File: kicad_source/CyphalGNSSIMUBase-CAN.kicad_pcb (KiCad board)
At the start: 2 copper layers, 52 x 36 mm, 39 parts, among them CN1 RASPBERRYPI_PICO, CN2 SM04B-SRSS-TB, CN3 SM04B-SRSS-TB, CN4 SM04B-GHS-TB, CN5 SM04B-GHS-TB, SW1 PTS636 SM43 SMTR LFS, U3 M24C64-RMN6TP, U8 MCP2515T-I/SO, U9 SN65HVD230, Y1 X322516MLB4SI

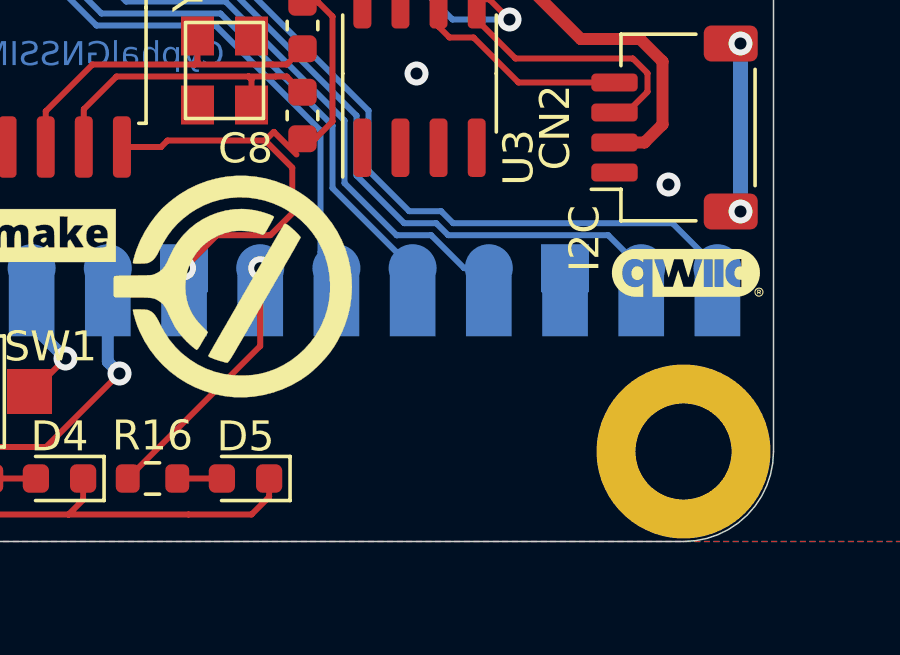
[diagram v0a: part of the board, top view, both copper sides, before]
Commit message: added BNO085
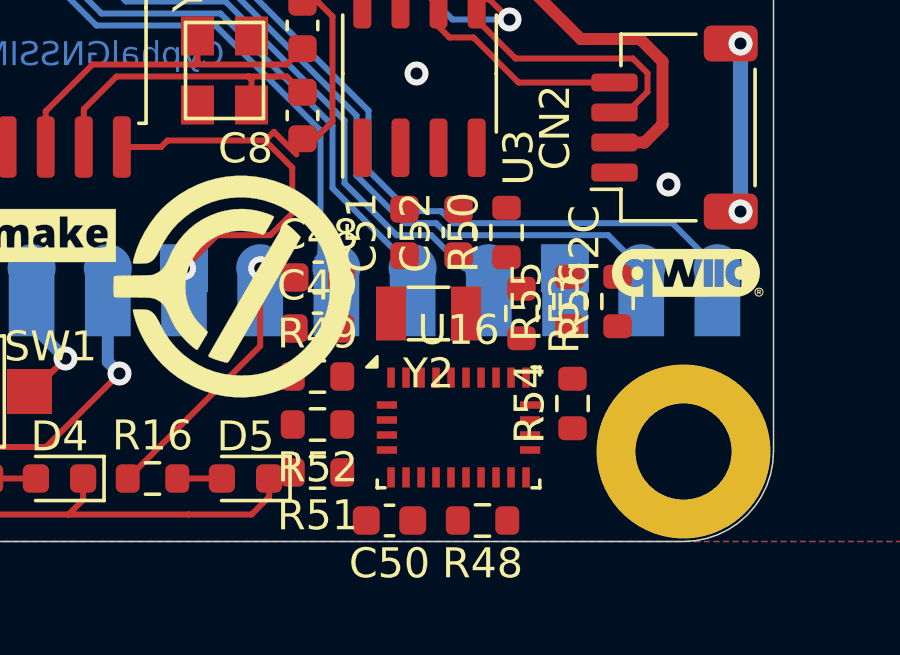
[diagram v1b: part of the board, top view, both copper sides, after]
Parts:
- added C48: 100nF, Capacitor_SMD:C_0603_1608Metric, F.Cu at (100.8, 101.2)
- added C49: 100nF, Capacitor_SMD:C_0603_1608Metric, F.Cu at (100.8, 102.9)
- added C50: 100nF, Capacitor_SMD:C_0603_1608Metric, F.Cu at (103.2, 109.3)
- added C51: 22pF, Capacitor_SMD:C_0603_1608Metric, F.Cu at (103.7, 99.7)
- added C52: 22pF, Capacitor_SMD:C_0603_1608Metric, F.Cu at (105.5, 99.7)
- added R48: 0R, Resistor_SMD:R_0603_1608Metric, F.Cu at (106.3, 109.3)
- added R49: 10k, Resistor_SMD:R_0603_1608Metric, F.Cu at (100.8, 104.5)
- added R50: 0R, Resistor_SMD:R_0603_1608Metric, F.Cu at (107.1, 99.7)
- added R51: 0R, Resistor_SMD:R_0603_1608Metric, F.Cu at (100.8, 107.7)
- added R52: 0R, Resistor_SMD:R_0603_1608Metric, F.Cu at (100.8, 106.1)
- added R53: DNI, Resistor_SMD:R_0603_1608Metric, F.Cu at (107.6, 102.4)
- added R54: 0R, Resistor_SMD:R_0603_1608Metric, F.Cu at (109.3, 105.4)
- added R55: DNI, Resistor_SMD:R_0603_1608Metric, F.Cu at (109.2, 102.0)
- added R56: DNI, Resistor_SMD:R_0603_1608Metric, F.Cu at (110.8, 102.0)
- added U16: BNO085, Package_LGA:LGA-28_5.2x3.8mm_P0.5mm, F.Cu at (105.5, 106.2)
- added Y2: DNI, Crystal:Crystal_SMD_3215-2Pin_3.2x1.5mm, F.Cu at (104.5, 102.4)
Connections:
- net /I2C_SCL renamed I2C_SCL
- net /I2C_SDA renamed I2C_SDA
- D2 pad 1: Net-(D2-K) -> (no net)
- F1 pad 2: Net-(D2-K) -> (no net)
- U9 pad 5: unconnected-(U9-NC2-Pad5) -> (no net)
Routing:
- net Net-(D2-K): track 4.26 -> 0.00 mm
- net (no net): track 6.35 -> 10.6 mm

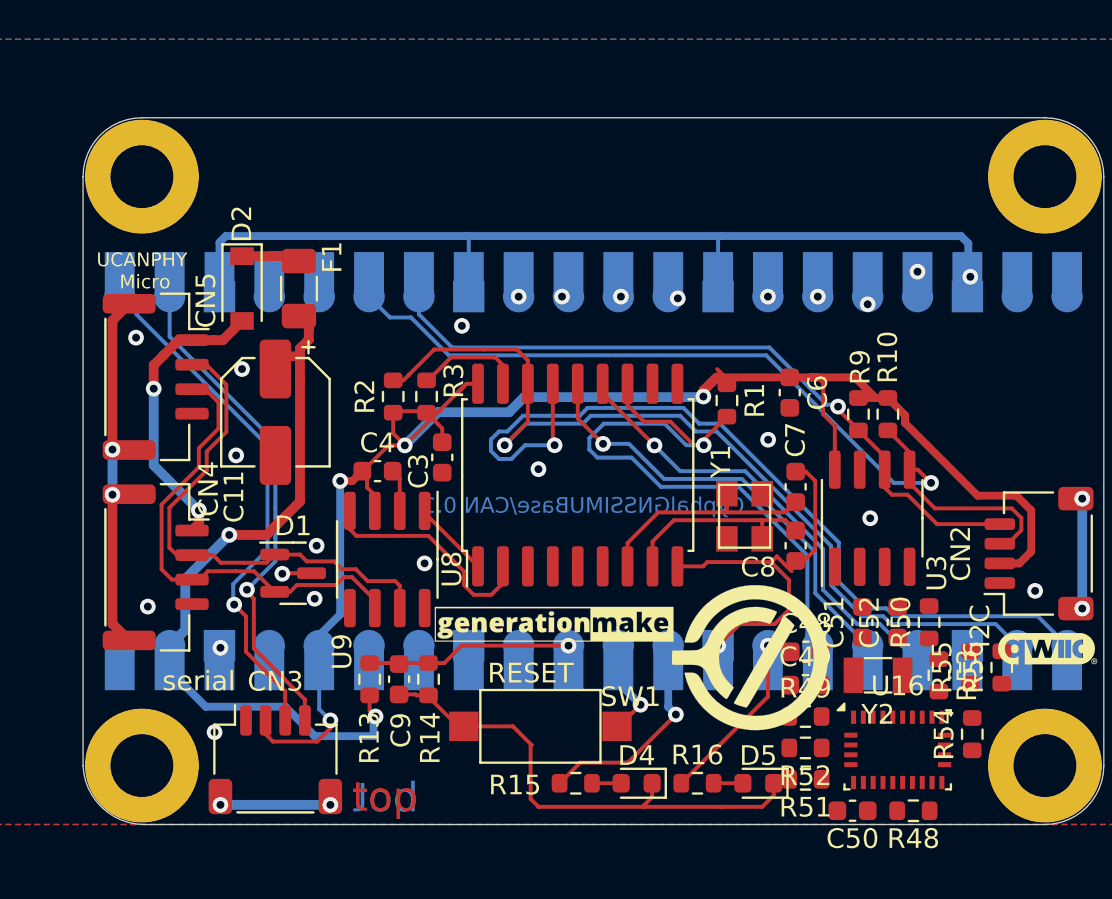
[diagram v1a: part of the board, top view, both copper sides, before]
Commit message: added GNSS u-blox max-m10
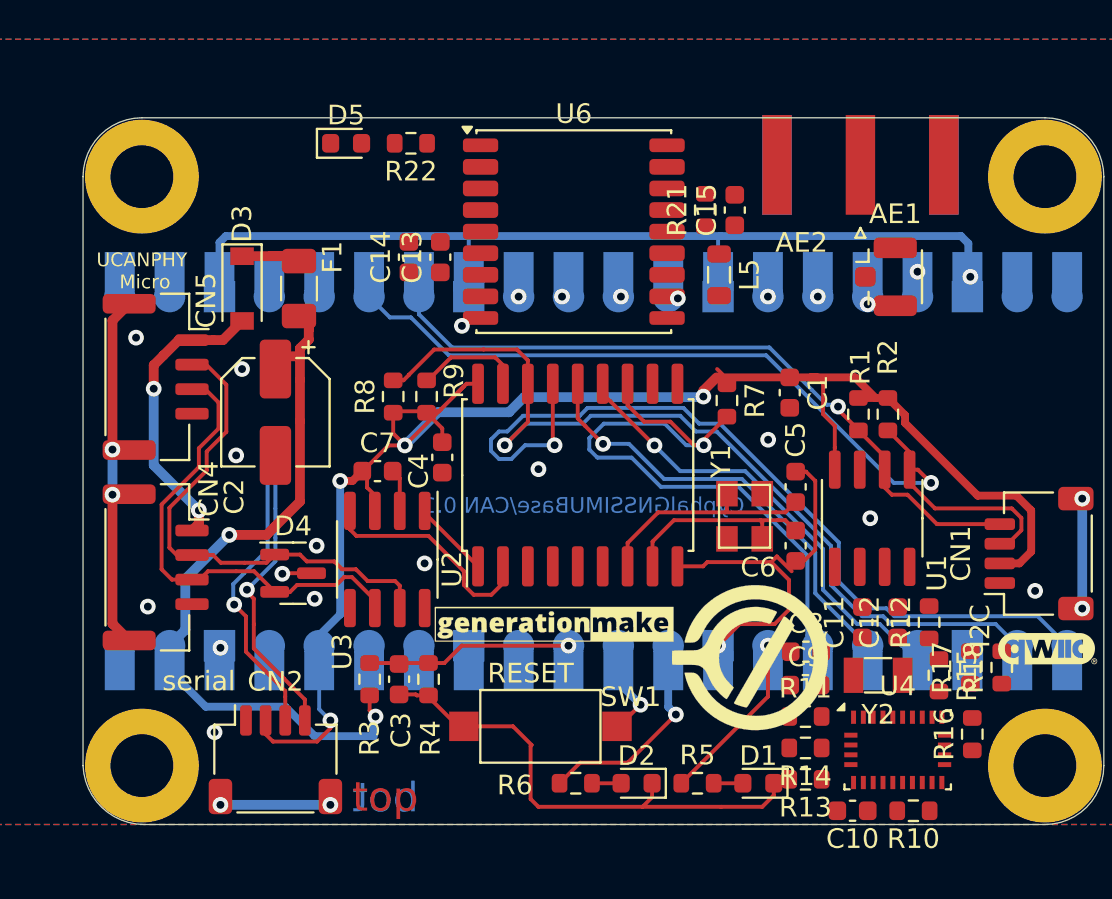
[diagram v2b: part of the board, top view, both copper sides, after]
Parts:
- added AE1: Antenna_Shield, Connector_Coaxial:U.FL_Hirose_U.FL-R-SMT-1_Vertical, F.Cu at (104.9, 82.1)
- added AE2: Antenna_Shield, Connector_Coaxial:SMA_Amphenol_132289_EdgeMount, F.Cu at (103.6, 76.4)
- added C13: 100 nF, Capacitor_SMD:C_0603_1608Metric, F.Cu at (82.2, 81.1)
- added C14: 100 nF, Capacitor_SMD:C_0603_1608Metric, F.Cu at (80.6, 81.1)
- added C15: 100 nF, Capacitor_SMD:C_0603_1608Metric, F.Cu at (97.2, 78.7)
- added D5: LED_Small, LED_SMD:LED_0603_1608Metric, F.Cu at (77.4, 75.3)
- added L5: L, Inductor_SMD:L_0805_2012Metric, F.Cu at (96.4, 82.0)
- added R21: 1k, Resistor_SMD:R_0603_1608Metric, F.Cu at (95.7, 78.7)
- added R22: 1k, Resistor_SMD:R_0603_1608Metric, F.Cu at (80.7, 75.3)
- added U6: MAX-M10S, RF_GPS:ublox_MAX, F.Cu at (89.0, 79.8)
- renumbered C6 to C1, C50 to C10, C51 to C11, C52 to C12, C11 to C2, C9 to C3, C3 to C4, C7 to C5, C8 to C6, C4 to C7, C48 to C8, C49 to C9, CN2 to CN1, CN3 to CN2, CN1 to CN3, D5 to D1, D4 to D2, D2 to D3, D1 to D4, R9 to R1, R48 to R10, R49 to R11, R50 to R12, R51 to R13, R52 to R14, R53 to R15, R54 to R16, R55 to R17, R56 to R18, R10 to R2, R13 to R3, R14 to R4, R16 to R5, R15 to R6, R1 to R7, R2 to R8, R3 to R9, U3 to U1, U8 to U2, U9 to U3, U16 to U4
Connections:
- CN2 pad 3: /SER_TX -> /SERIAL2_TX
- CN2 pad 4: /SER_RX -> /SERIAL2_RX
- CN3 pad 1: /SER_TX -> SERIAL1_TX
- CN3 pad 11: /INPUT2 -> /SERIAL2_TX
- CN3 pad 12: /INPUT3 -> /SERIAL2_RX
- CN3 pad 2: /SER_RX -> SERIAL1_RX
- D3 pad 1: (no net) -> Net-(D3-K)
- F1 pad 2: (no net) -> Net-(D3-K)
- U3 pad 5: (no net) -> unconnected-(U3-NC2-Pad5)
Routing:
- net /SER_TX: track 27.8 -> 0.00 mm, vias 1 -> 0
- net /SER_RX: track 27.0 -> 0.00 mm, vias 1 -> 0
- net /SERIAL2_TX: track 0.00 -> 17.1 mm, vias 0 -> 2
- net /SERIAL2_RX: track 0.00 -> 16.0 mm, vias 0 -> 1
- net Net-(D3-K): track 0.00 -> 4.26 mm
- net (no net): track 10.6 -> 6.35 mm
- net SERIAL1_TX: track 0.00 -> 1.27 mm
- net SERIAL1_RX: track 0.00 -> 1.27 mm
- net /INPUT3: track 1.27 -> 0.00 mm, vias 1 -> 0
- net /INPUT2: track 1.27 -> 0.00 mm, vias 1 -> 0
- net /GNSS/NEO_ANTENNA: track 0.00 -> 1.27 mm, vias 0 -> 1

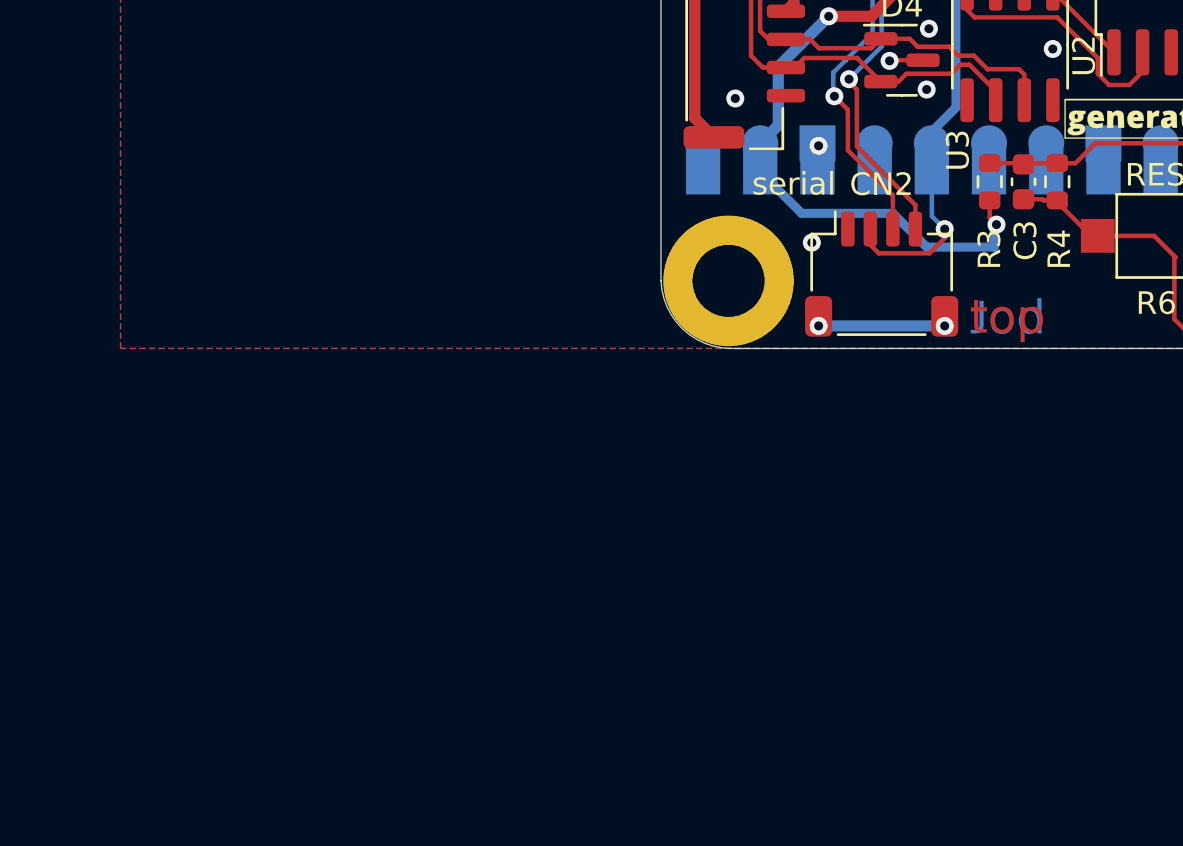
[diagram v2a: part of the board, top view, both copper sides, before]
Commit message: added RS232 level shifter
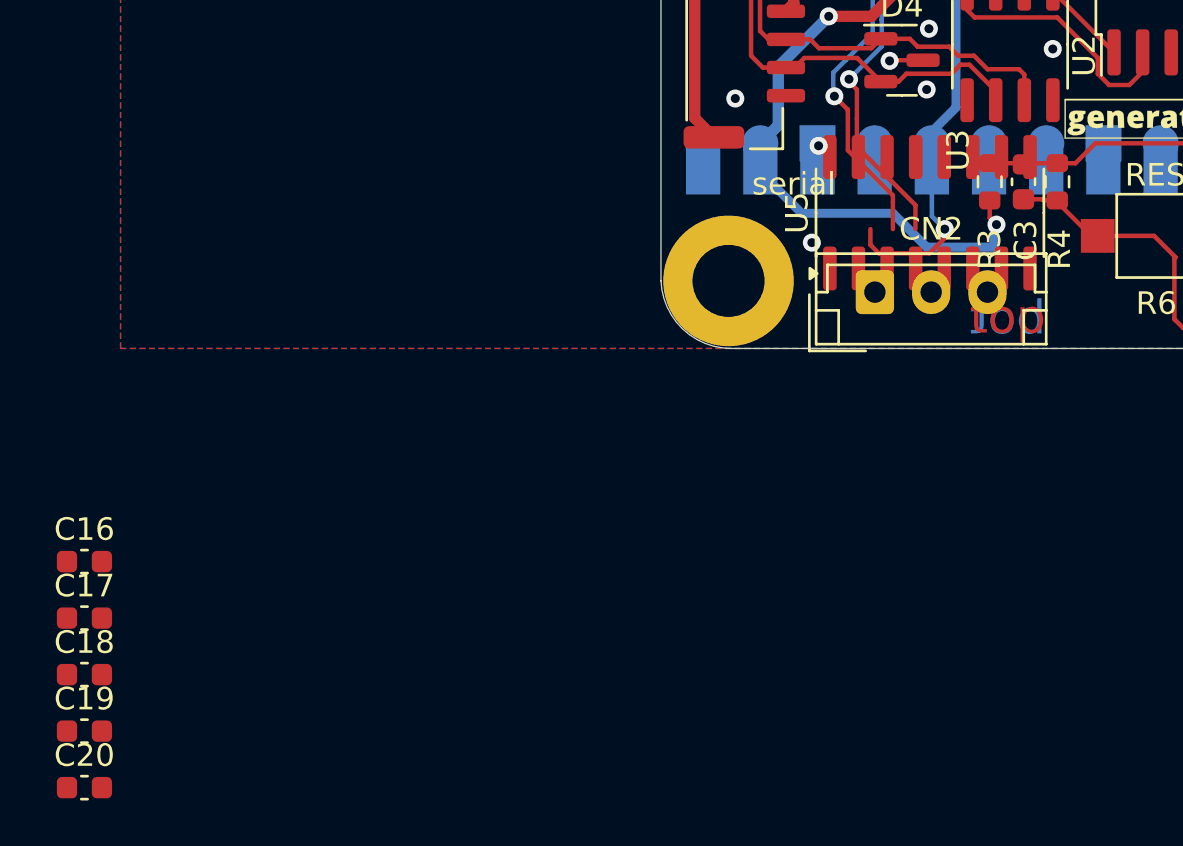
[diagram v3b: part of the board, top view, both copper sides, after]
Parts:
- added C16: 100nF, Capacitor_SMD:C_0603_1608Metric, F.Cu at (38.4, 119.5)
- added C17: 100nF, Capacitor_SMD:C_0603_1608Metric, F.Cu at (38.4, 122.0)
- added C18: 100nF, Capacitor_SMD:C_0603_1608Metric, F.Cu at (38.4, 124.5)
- added C19: 100nF, Capacitor_SMD:C_0603_1608Metric, F.Cu at (38.4, 127.0)
- added C20: 100nF, Capacitor_SMD:C_0603_1608Metric, F.Cu at (38.4, 129.5)
- added U5: MAX3232, Package_SO:SOIC-16_3.9x9.9mm_P1.27mm, F.Cu at (75.9, 104.0)
- CN2: value SM04B-SRSS-TB -> Conn_01x03; footprint generationmake:JST_SH_SM04B-SRSS-TB_1x04-1MP_P1.00mm_Horizontal -> Connector_JST:JST_EH_B3B-EH-A_1x03_P2.50mm_Vertical
- moved CN2 0.85 mm to (73.5, 107.5)
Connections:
- CN2 pad 1: GND -> /RS232_TX
- CN2 pad 2: +3V3 -> GND
- CN2 pad 3: /SERIAL2_TX -> /RS232_TX
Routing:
- net /MP3: track 5.60 -> 0.00 mm, vias 2 -> 0

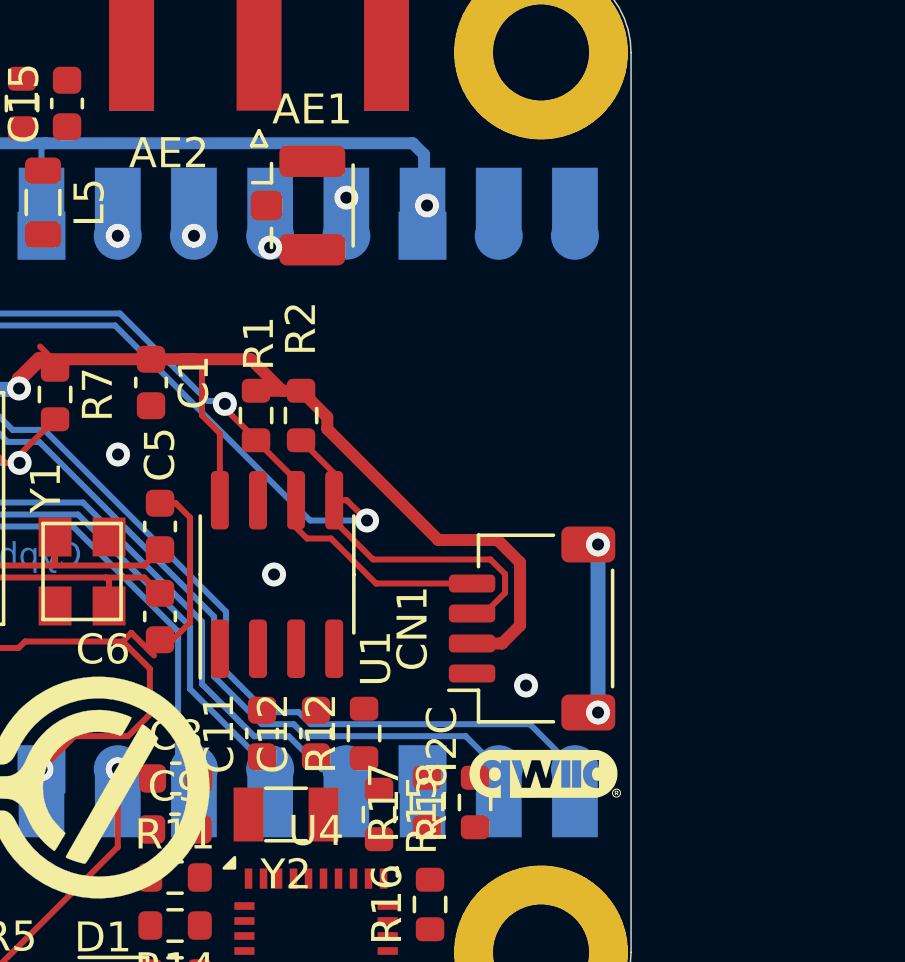
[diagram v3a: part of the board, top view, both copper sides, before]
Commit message: added battery holder for GNSS backup
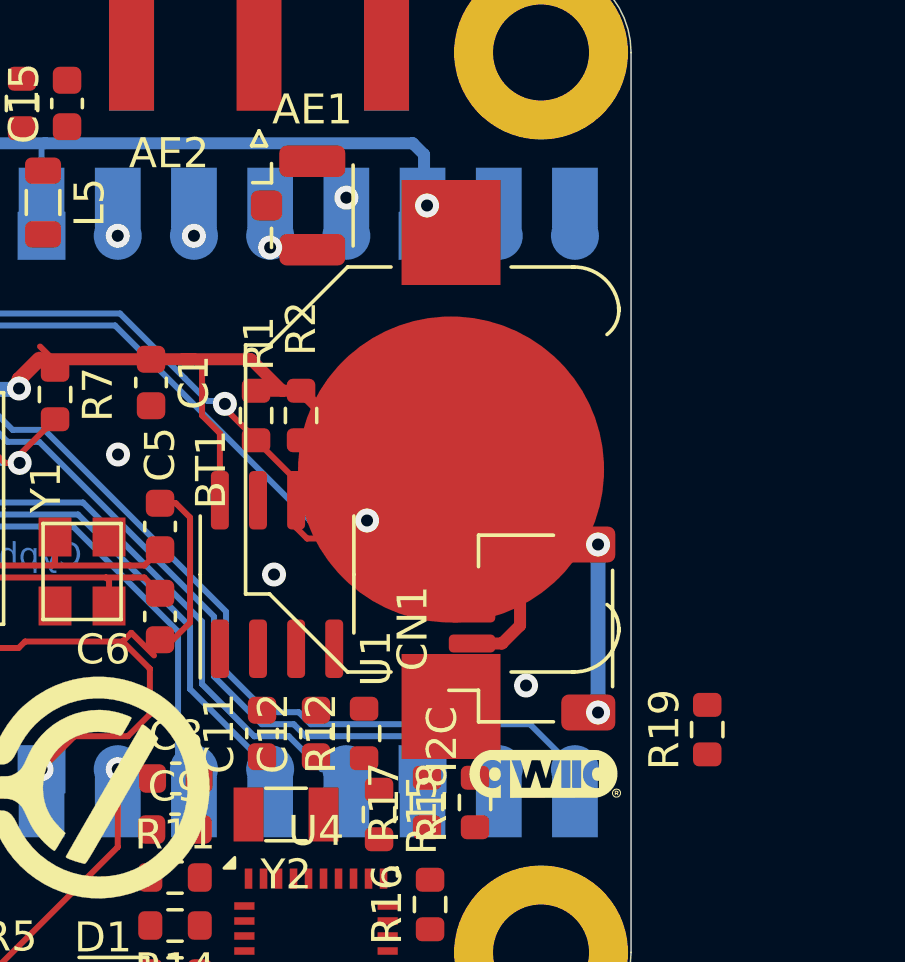
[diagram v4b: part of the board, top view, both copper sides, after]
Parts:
- added BT1: Battery_Cell, Battery:BatteryHolder_Keystone_3000_1x12mm, F.Cu at (110.0, 90.9)
- added R19: 1k, Resistor_SMD:R_0603_1608Metric, F.Cu at (118.5, 99.6)
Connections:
- U6 pad 6: unconnected-(U6-V_BCKP-Pad6) -> /GNSS/V_BCKP
